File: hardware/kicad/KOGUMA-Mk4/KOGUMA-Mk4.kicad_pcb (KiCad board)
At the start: 2 copper layers, 75.6 x 69.2 mm, 143 parts, among them J1 BATT (BT2.0), J2 MOTOR_L, J3 MOTOR_R, J4 FAN, J5 ENC_L, J6 ENC_R, J7 DEBUG (STLINK-V3MODS), Q1 AO4407A, Q40 IRLML6344, Q90 2N7002, SW1 SSSS810701, SW2 TVAF06-A020B-R, U1 LXDC55FAAA-203, U2 MP6551GQB, U3 MP6551GQB, U4 STM32H725RGVx, U70 NJU6080, U71 NJU6080, U72 NJU6080, U73 NJU6080, U74 OPA2354, U75 OPA2354, U76 LSM6DSR, Y1 CSTNE10M0G52Z000R0

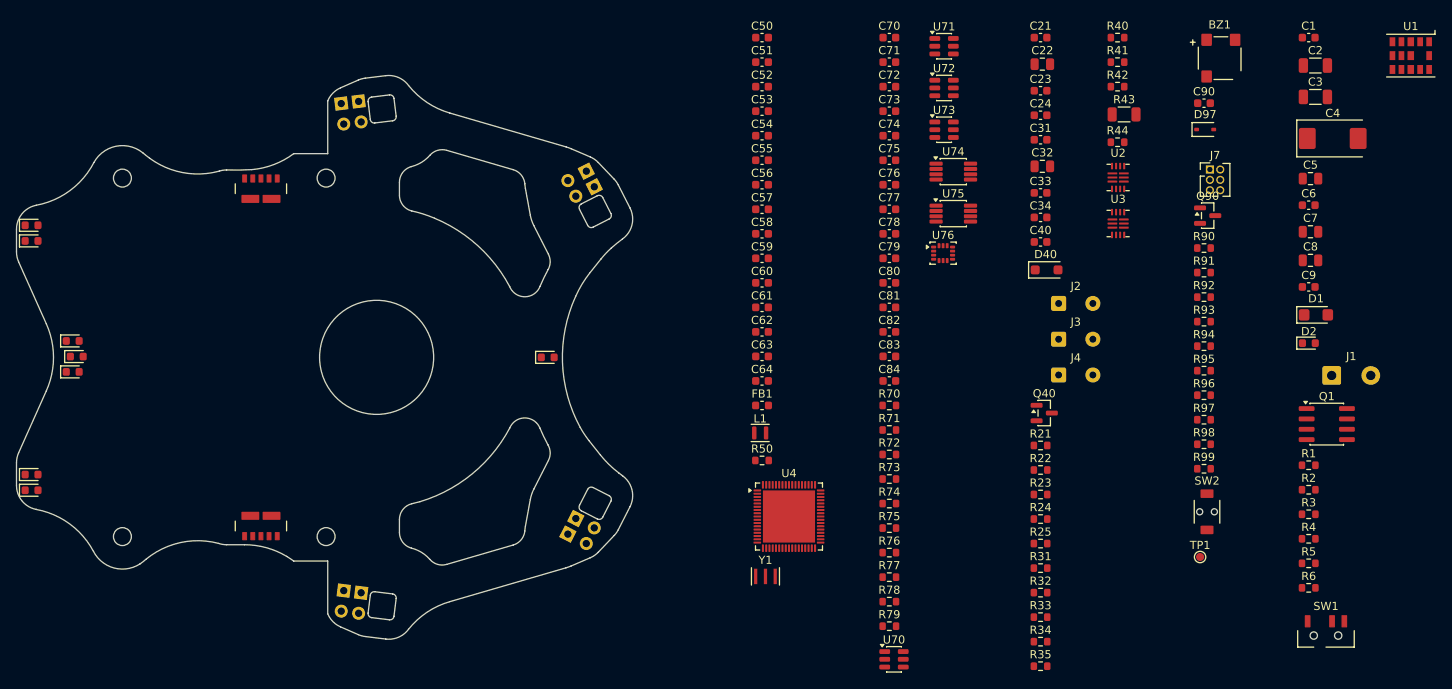
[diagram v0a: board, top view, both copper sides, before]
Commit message: メイン基板の部品を置く(最初の案)。基板を v17 に(ポケットのまわりを 5.5mm)
- 部品はすべて表、電池は部品の上(電池の下は高さ 1.1mm 以下だけ)。機体のモデルから基板の上下のすき間を測った
- place_pcb.py: IC・コネクタはまとまりごとに、抵抗・コンデンサはつながる IC のパッドのそばの空いている所へ
- 電源スイッチは後ろの V 字の左の斜めの縁、押しボタンは電池の左、デバッグ端子は電池の右、ブザーは前の真ん中
- 受光アンプが縁に入らなかったので、ポケットのまわりに残す幅を 4.5 → 5.5mm(+0.13g、1次 153Hz)
- DRC: 部品の重なり 0、回路図との食い違い 0(残りはシルクが縁にかかる所だけ)

Co-Authored-By: Claude Opus 5.5 <noreply@anthropic.com>
Claude-Session: https://claude.ai/code/session_01H2Zvpqxqu2v63zaiCMmfT3
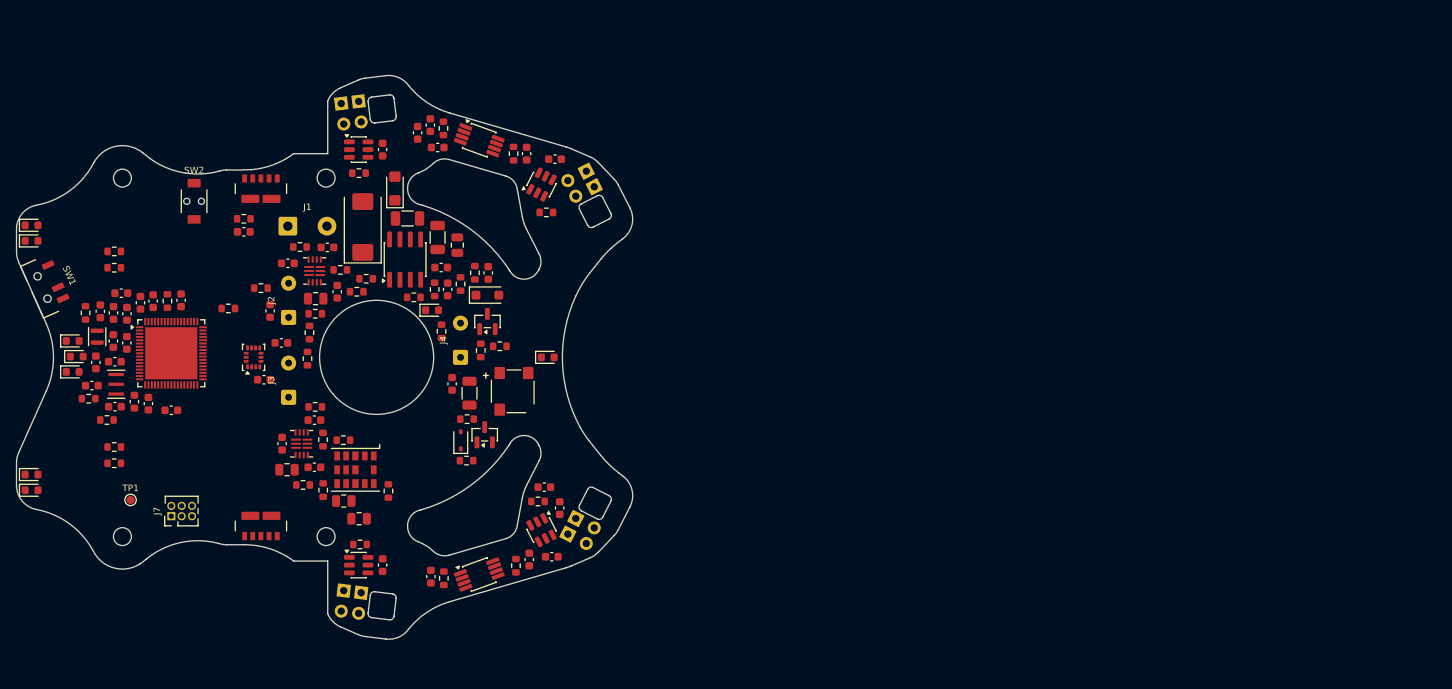
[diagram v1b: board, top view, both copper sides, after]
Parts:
- moved SW1 163.2 mm to (123.2, 91.4), turned to -66 degrees
- moved U1 139.1 mm to (161.6, 113.8)
- moved R90 138.1 mm to (128.9, 105.1)
- moved R92 137.3 mm to (128.5, 94.5), turned to 90 degrees
- moved R91 135.9 mm to (131.1, 107.7)
- moved R96 134.9 mm to (132.0, 87.0)
- moved R93 134.6 mm to (132.0, 111.0)
- moved R94 134.5 mm to (132.0, 113.0)
- moved J7 134.4 mm to (139.0, 119.5), turned to 90 degrees
- moved R95 134.3 mm to (132.0, 89.0)
- moved TP1 131.5 mm to (134.0, 117.5)
- moved SW2 130.0 mm to (141.8, 80.8)
- moved J1 129.4 mm to (153.3, 83.9)
- moved C9 127.5 mm to (151.1, 94.3), turned to 90 degrees
- moved R5 125.4 mm to (155.7, 100.2), turned to 90 degrees
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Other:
- outline, holes or cut-outs redrawn

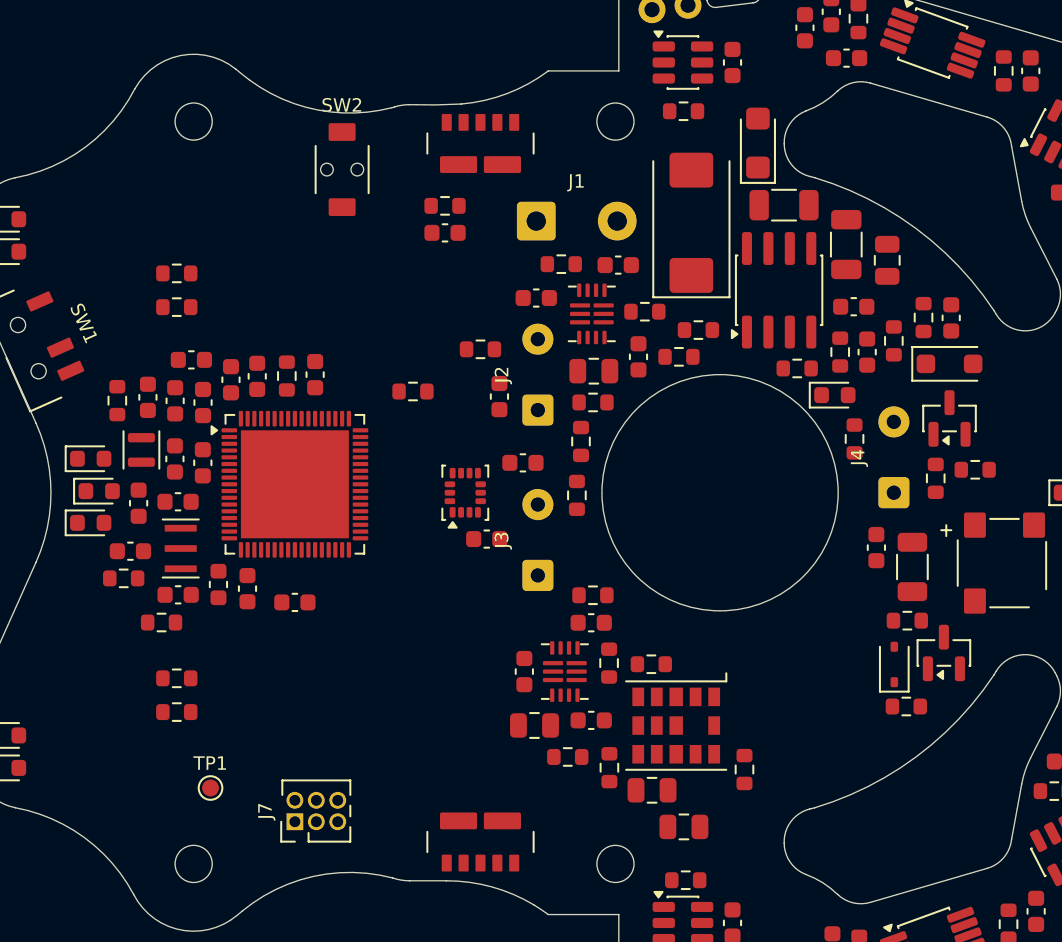
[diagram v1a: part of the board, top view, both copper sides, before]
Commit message: 配置を後ろから 電源 → モータードライバ → マイコン の順に。電池の下を 2.1mm まで(電池を持ち上げる)
- 電源(電池の線・スイッチの FET・大きいコンデンサ・DC-DC)を電池の下の後ろ、ドライバを真ん中、MCU を前の端(180°)
- 背の高い電源の部品(タンタル 2.0mm・SO-8)を電池の下に入れるため、電池を 2.1mm 持ち上げる(vehicle.py の BAT_LIFT)
- 押しボタン・電源スイッチ・デバッグ端子・ブザーは電池の外。線のパッドははんだが低いので電池の下でよい
- DRC: 部品の重なり 0、回路図との食い違い 0

Co-Authored-By: Claude Opus 5.5 <noreply@anthropic.com>
Claude-Session: https://claude.ai/code/session_01H2Zvpqxqu2v63zaiCMmfT3
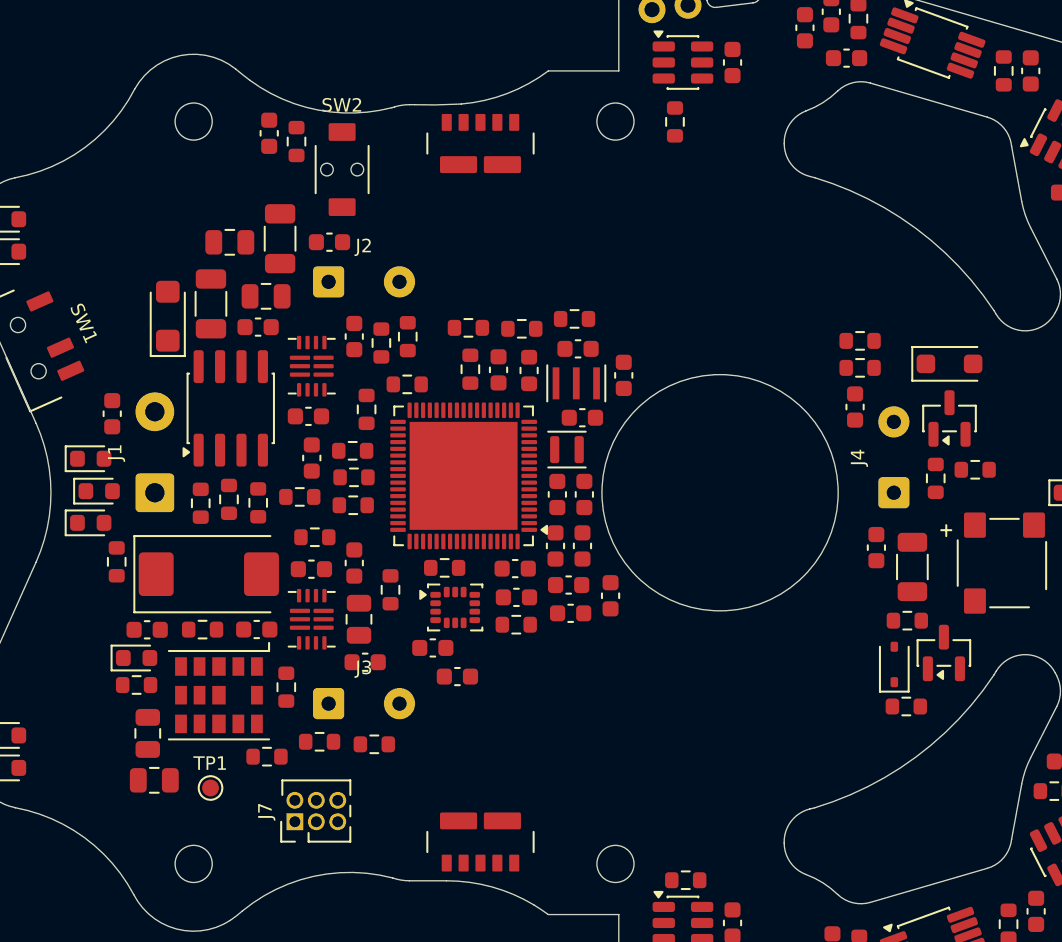
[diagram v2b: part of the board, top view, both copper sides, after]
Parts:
- moved R6 45.0 mm to (129.6, 111.4), turned to 0 degrees
- moved C1 44.9 mm to (128.2, 95.3)
- moved D2 44.2 mm to (129.6, 109.8)
- moved C5 39.0 mm to (135.1, 85.2), turned to 0 degrees
- moved C2 37.8 mm to (134.0, 88.8)
- moved R1 37.3 mm to (135.1, 100.4)
- moved D1 36.5 mm to (131.5, 89.5)
- moved R2 36.2 mm to (133.4, 100.6), turned to 90 degrees
- moved C4 35.4 mm to (133.9, 104.8), turned to 0 degrees
- moved Q1 33.2 mm to (135.2, 95.0)
- moved C8 31.5 mm to (130.7, 117.0)
- moved C6 31.3 mm to (141.0, 85.1)
- moved C63 31.0 mm to (158.5, 93.0), turned to 90 degrees
- moved C7 30.1 mm to (130.3, 114.3), turned to 90 degrees
- moved C3 29.9 mm to (138.1, 84.9), turned to 90 degrees
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
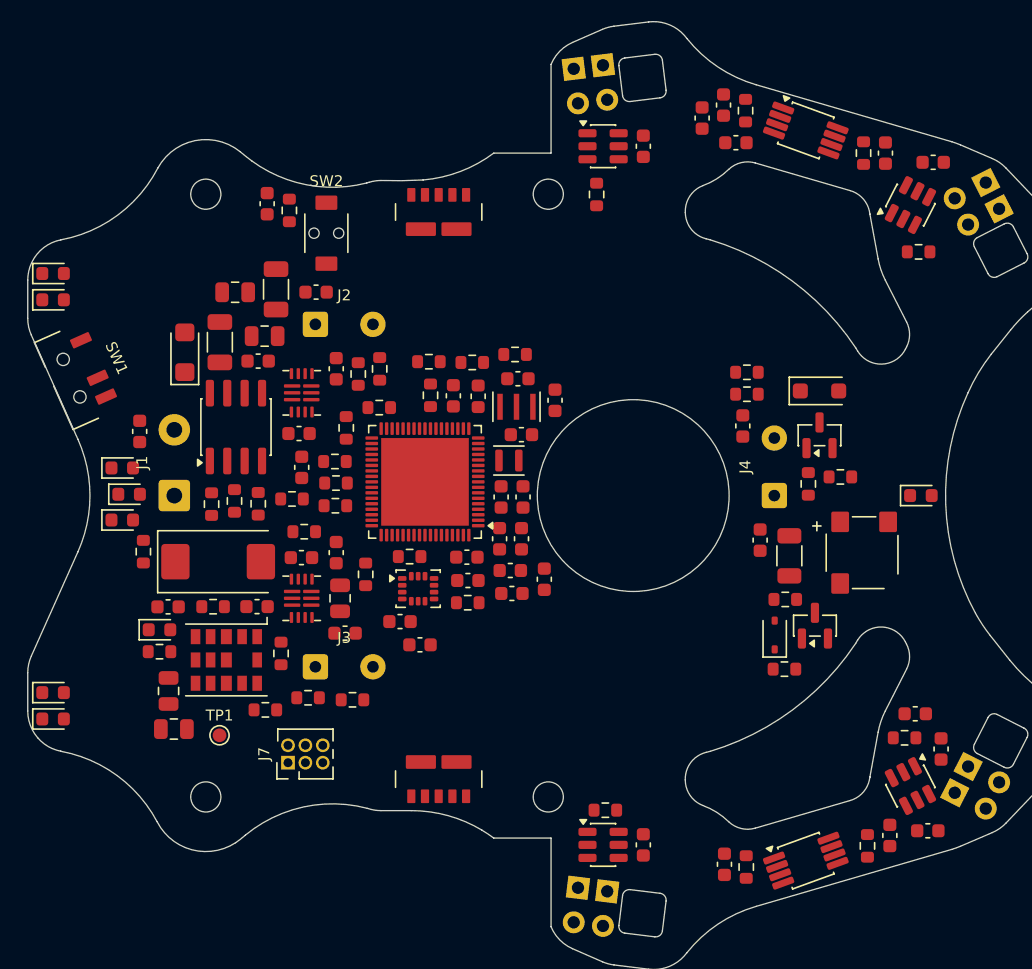
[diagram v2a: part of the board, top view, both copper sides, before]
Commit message: 置き直し: IC のまわりに線の通り道を空け、部品どうしに 0.25mm のすき間(全部の部品が入った)
MCU のまわり 2.5mm はパスコン・発振子・SMPS だけ、LED の抵抗は LED のそば。DRC: 部品の重なり 0、回路図との食い違い 0

Co-Authored-By: Claude Opus 5.5 <noreply@anthropic.com>
Claude-Session: https://claude.ai/code/session_01H2Zvpqxqu2v63zaiCMmfT3
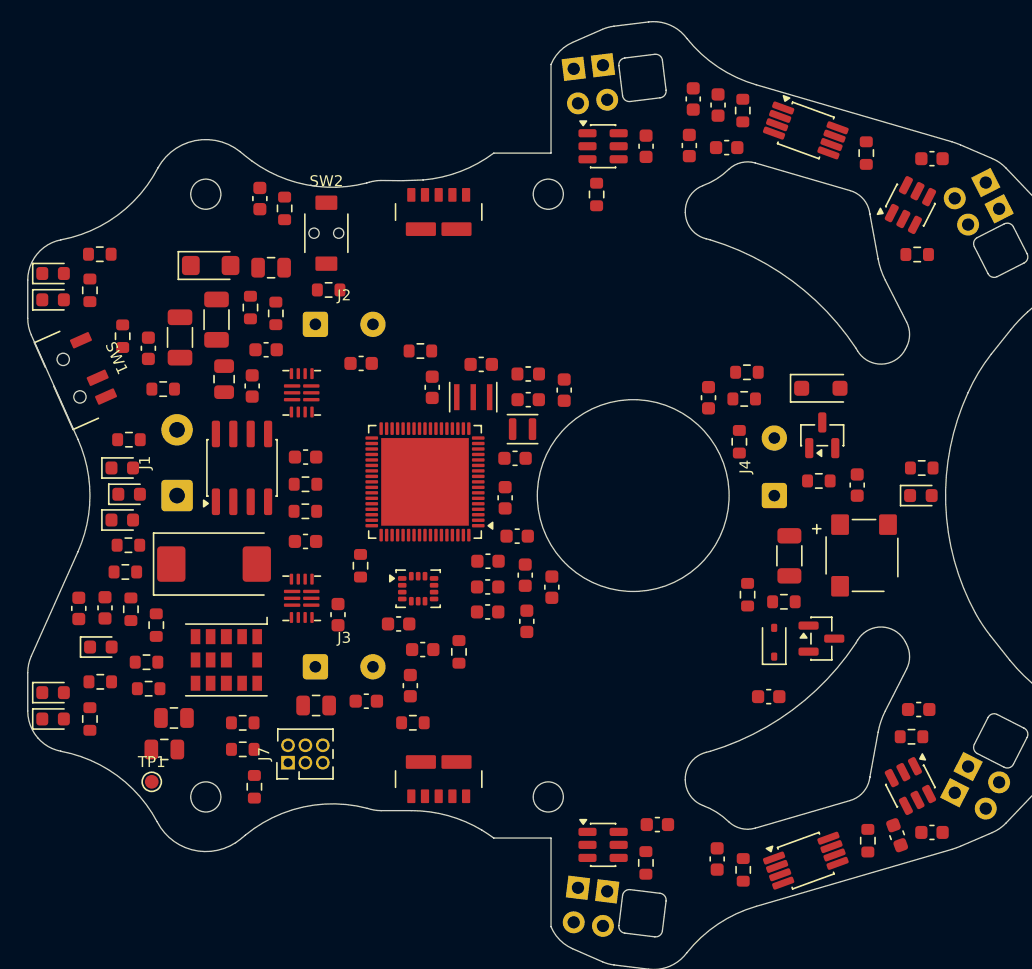
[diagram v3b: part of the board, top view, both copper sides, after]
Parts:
- moved R99 37.9 mm to (185.3, 98.0)
- moved R93 36.0 mm to (124.5, 116.3), turned to 90 degrees
- moved R94 28.6 mm to (125.3, 113.6)
- moved R90 28.4 mm to (127.3, 103.6)
- moved R92 25.8 mm to (129.9, 92.2)
- moved R96 22.9 mm to (125.3, 82.4)
- moved R91 22.3 mm to (127.4, 95.9), turned to 0 degrees
- moved R95 21.2 mm to (124.5, 85.0)
- moved R4 20.8 mm to (126.9, 88.4), turned to 90 degrees
- moved R33 15.7 mm to (129.4, 109.5)
- moved R40 14.3 mm to (136.3, 86.3)
- moved R32 14.3 mm to (151.5, 111.4), turned to 90 degrees
- moved C1 13.1 mm to (125.6, 108.2)
- moved C6 12.9 mm to (128.8, 89.2), turned to 90 degrees
- moved R25 12.9 mm to (148.7, 89.4)
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
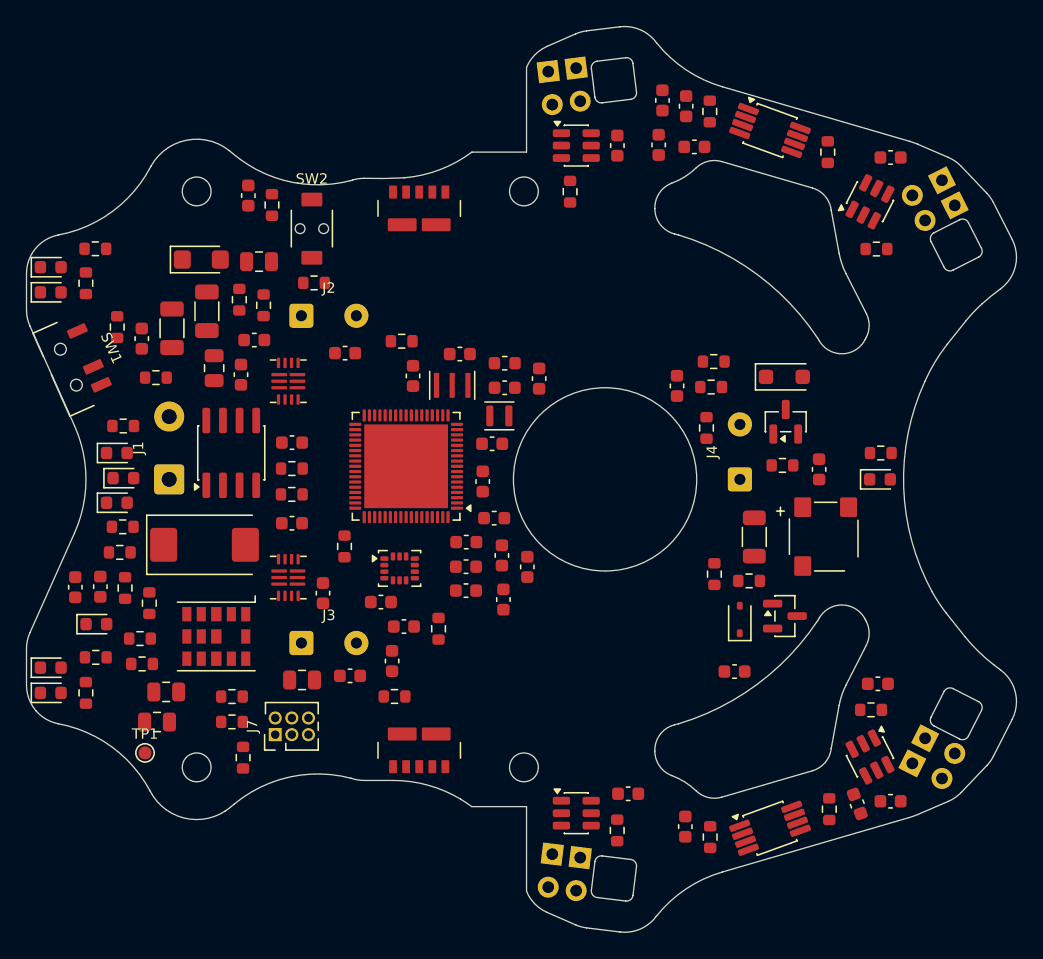
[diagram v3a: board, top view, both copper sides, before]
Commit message: 自動配線の4回目(線・クリアランス 0.15mm): GND 以外で残り 38 本。基板のファイルを途中の配線にする
Co-Authored-By: Claude Opus 5.5 <noreply@anthropic.com>
Claude-Session: https://claude.ai/code/session_01H2Zvpqxqu2v63zaiCMmfT3
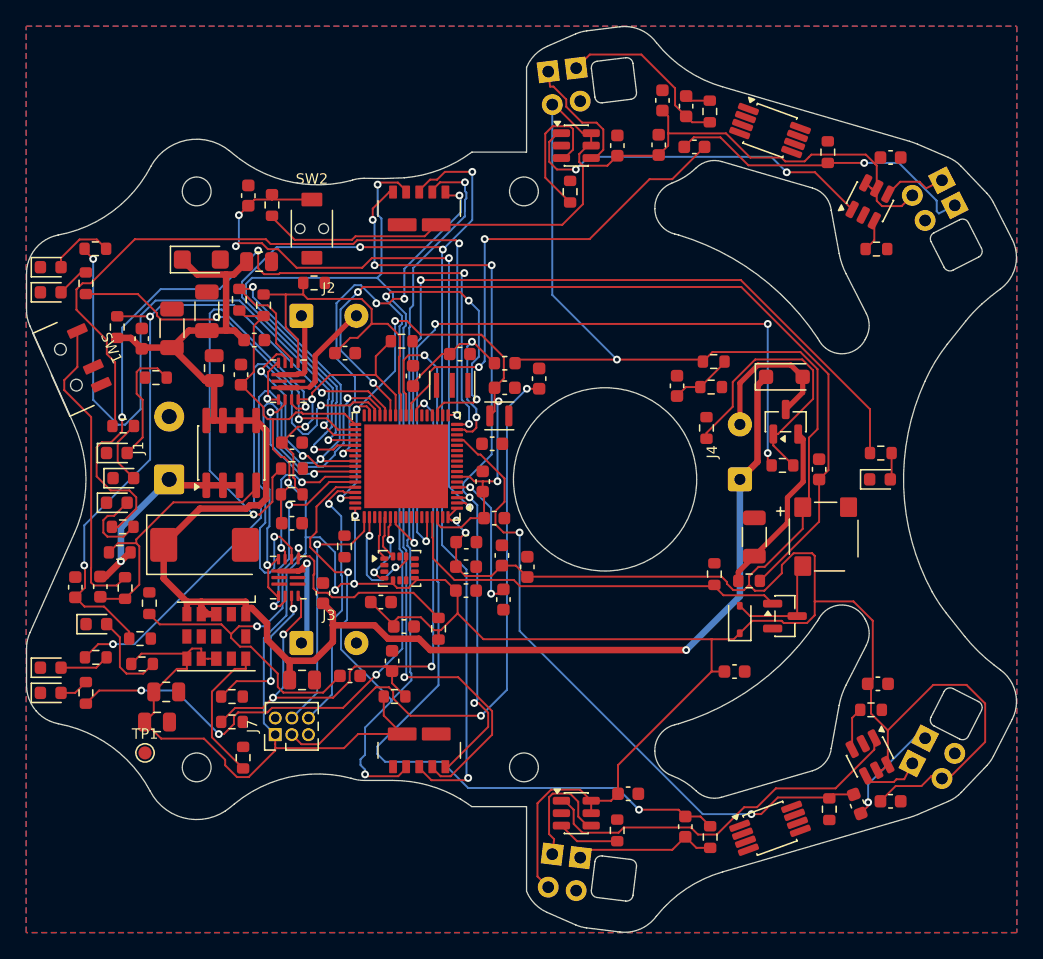
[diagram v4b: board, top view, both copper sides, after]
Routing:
- net +3V3: track 0.00 -> 401.9 mm, vias 0 -> 7
- net VBAT: track 0.00 -> 127.1 mm, vias 0 -> 1
- net ENC_MOSI: track 0.00 -> 93.2 mm, vias 0 -> 5
- net ENC_MISO: track 0.00 -> 84.8 mm, vias 0 -> 3
- net ENC_SCK: track 0.00 -> 77.6 mm, vias 0 -> 3
- net LED_NUM0: track 0.00 -> 75.3 mm, vias 0 -> 6
- net FAN_ISENSE: track 0.00 -> 68.4 mm, vias 0 -> 2
- net WALL_FR: track 0.00 -> 66.6 mm, vias 0 -> 2
- net LED_FRONT: track 0.00 -> 64.7 mm, vias 0 -> 2
- net LED_MODE0: track 0.00 -> 62.5 mm, vias 0 -> 4
- net ENC_CAL: track 0.00 -> 58.2 mm, vias 0 -> 5
- net MOT_nFAULT: track 0.00 -> 57.1 mm, vias 0 -> 3
- net LED_MODE1: track 0.00 -> 56.8 mm, vias 0 -> 2
- net FAN_PWM: track 0.00 -> 55.7 mm, vias 0 -> 4
- net BATT: track 0.00 -> 54.4 mm, vias 0 -> 3
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- added copper zone on B.Cu, net GND
- added copper zone on F.Cu, net GND
